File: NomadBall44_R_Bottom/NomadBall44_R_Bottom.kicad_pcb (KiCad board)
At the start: 2 copper layers, 144.8 x 96.5 mm, 0 parts

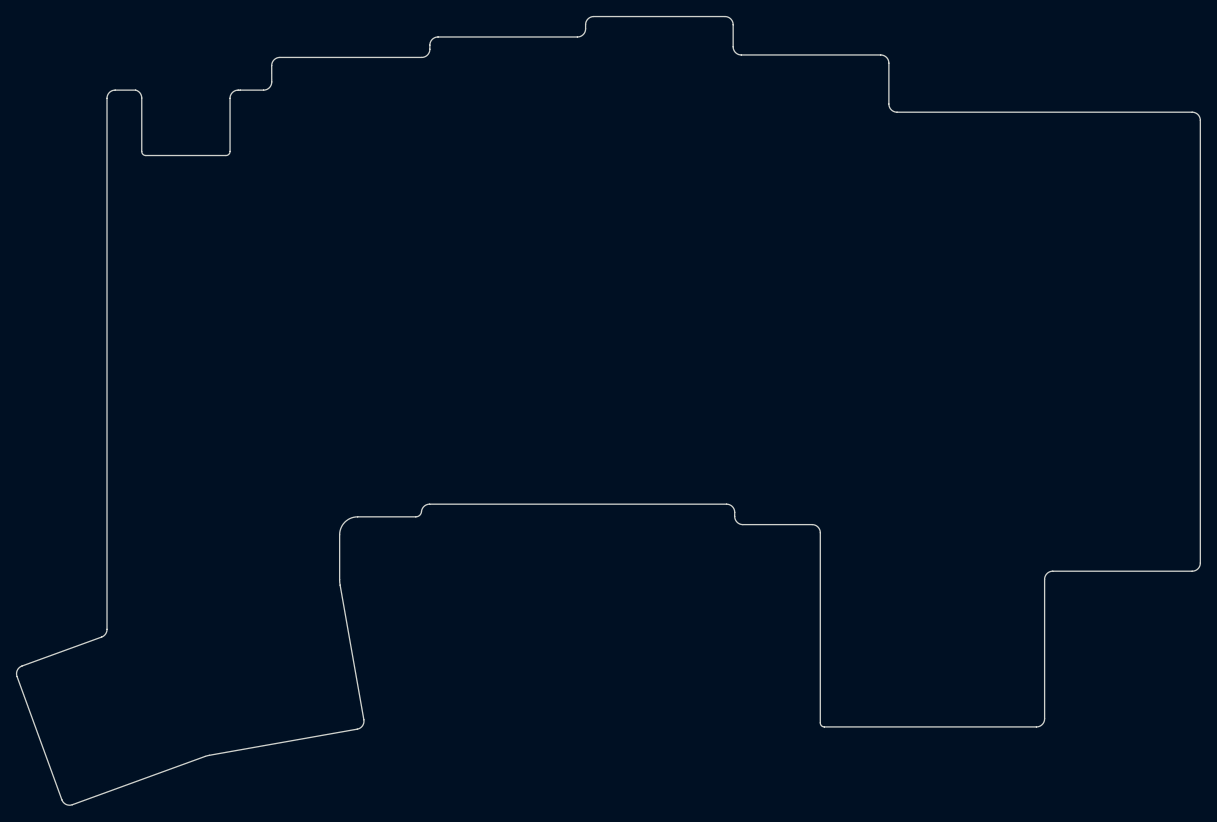
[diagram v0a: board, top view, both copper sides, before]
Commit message: ボトムプレートの作成
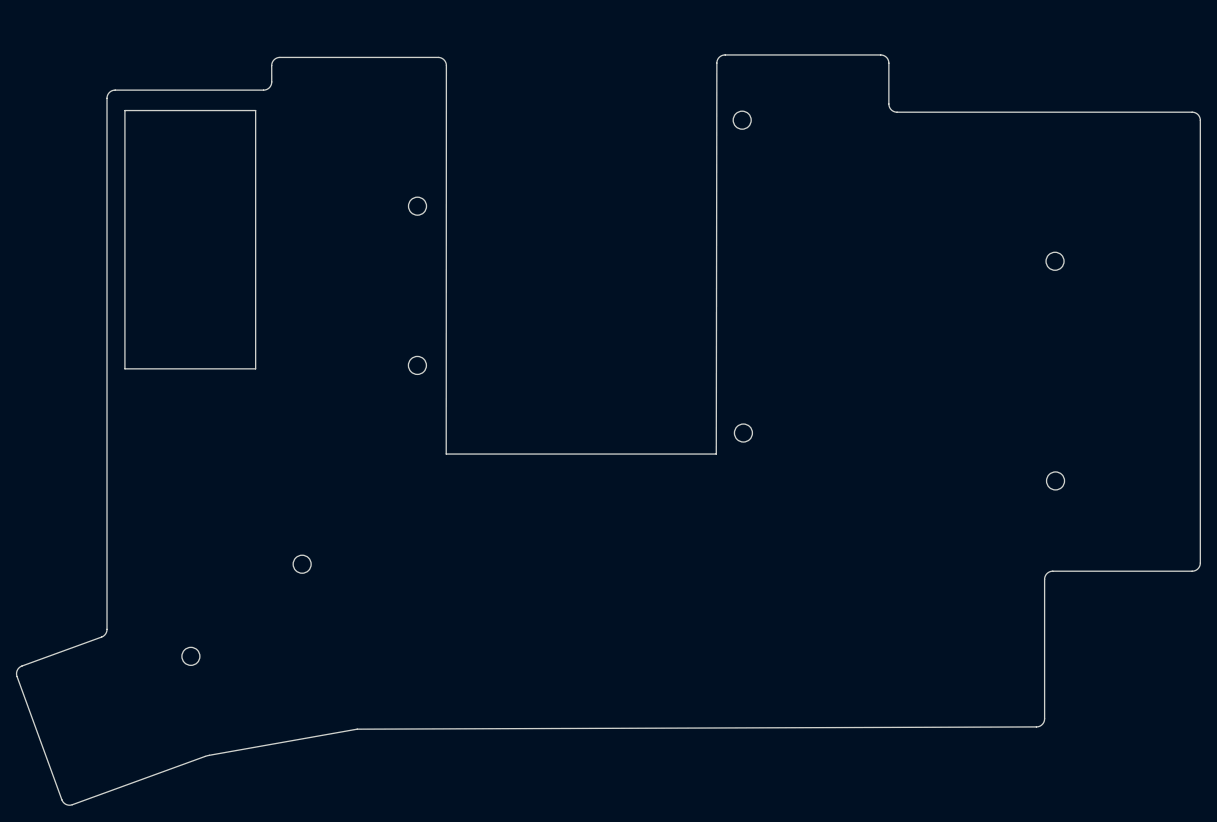
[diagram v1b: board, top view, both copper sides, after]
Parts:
- added REF**: Val**, NomadBall44:m2_Screw_Hole_EdgeCuts, F.Cu at (163.4, 91.7)
- added REF**: Val**, NomadBall44:m2_Screw_Hole_EdgeCuts, F.Cu at (201.5, 97.5)
- added REF**: Val**, NomadBall44:m2_Screw_Hole_EdgeCuts, F.Cu at (123.5, 83.4)
- added REF**: Val**, NomadBall44:m2_Screw_Hole_EdgeCuts, F.Cu at (163.2, 53.4)
- added REF**: Val**, NomadBall44:m2_Screw_Hole_EdgeCuts, F.Cu at (109.4, 107.7)
- added REF**: Val**, NomadBall44:m2_Screw_Hole_EdgeCuts, F.Cu at (201.5, 70.7)
- added REF**: Val**, NomadBall44:m2_Screw_Hole_EdgeCuts, F.Cu at (123.5, 63.9)
- added REF**: Val**, NomadBall44:m2_Screw_Hole_EdgeCuts, F.Cu at (95.8, 119.0)
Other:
- board size 144.8 x 96.5 mm -> 144.8 x 91.8 mm
